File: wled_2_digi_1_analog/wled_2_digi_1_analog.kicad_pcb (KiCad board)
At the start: 2 copper layers, 100 x 38 mm, 54 parts, among them J1 Barrel_Jack_Switch, J2 Screw_Terminal_01x01, J3 Screw_Terminal_01x04, J4 Screw_Terminal_01x04, J5 Screw_Terminal_01x05, Q1 IRLR7843TR(UMW), Q2 AP15P04S, Q3 MMBT4401LT1G, Q4 MMBT4401LT1G, Q5 AP15P04S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

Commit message: Mounting Holes and 2pin connector
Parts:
- removed the ? at (111.0, 89.1)
- removed the ? at (102.0, 55.6)
- removed the ? at (139.5, 89.2)
- removed J2: Screw_Terminal_01x01, NicosLib:CONN-TH_P5.00_KF301-5.0-1P
- added ?: , , F.Cu at (70.2, 55.6)
- added ?: , , F.Cu at (102.1, 55.6)
- added ?: , , F.Cu at (139.5, 89.0)
- added U4: Screw Terminal, easyeda2kicad:CONN-TH_P5.00_KF301-5.0-2P, F.Cu at (71.5, 88.6)
- moved REF** 51.9 mm to (111.0, 89.0)
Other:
- board text added: "CH1"
- board text added: "CH2"
- board text added: "CH3"
- board text added: "CH4"
- board text added: "CH5"
- board text added: "V+ Analog"

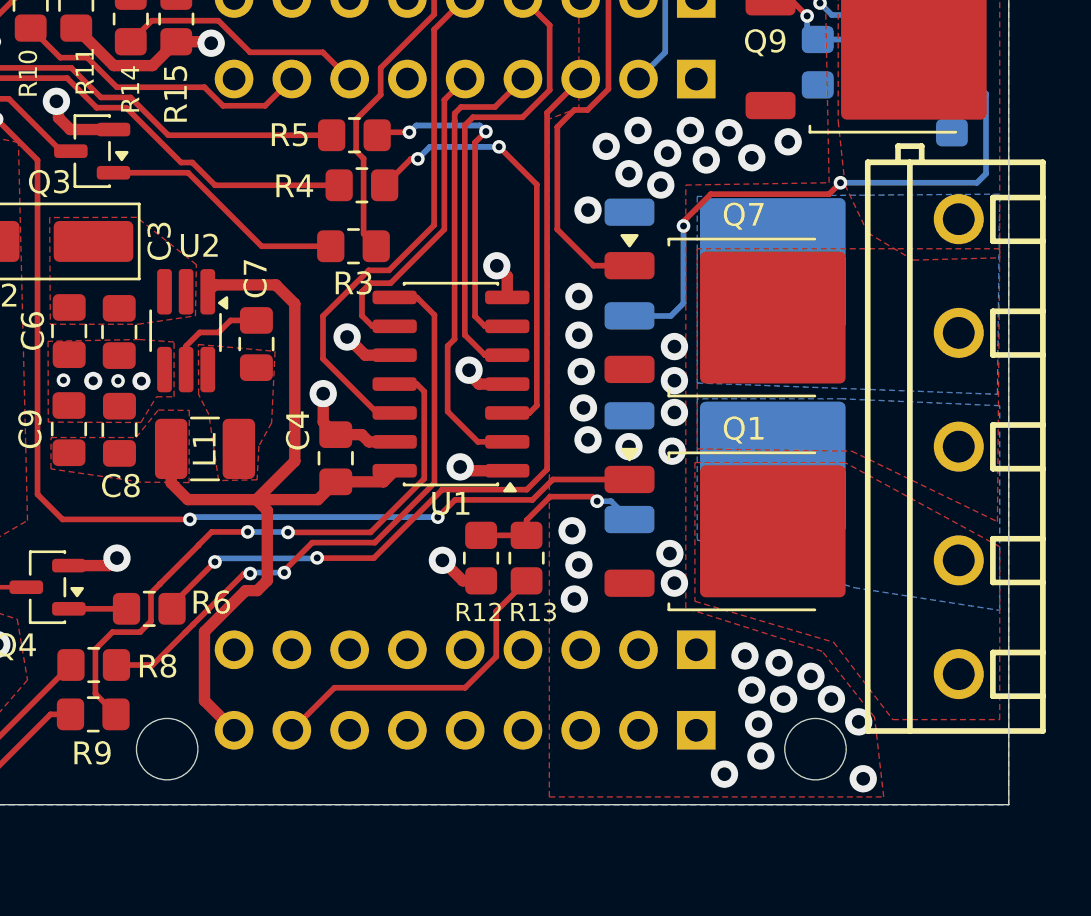
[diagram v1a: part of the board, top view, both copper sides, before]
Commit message: Switch 5pin to 2+3ping
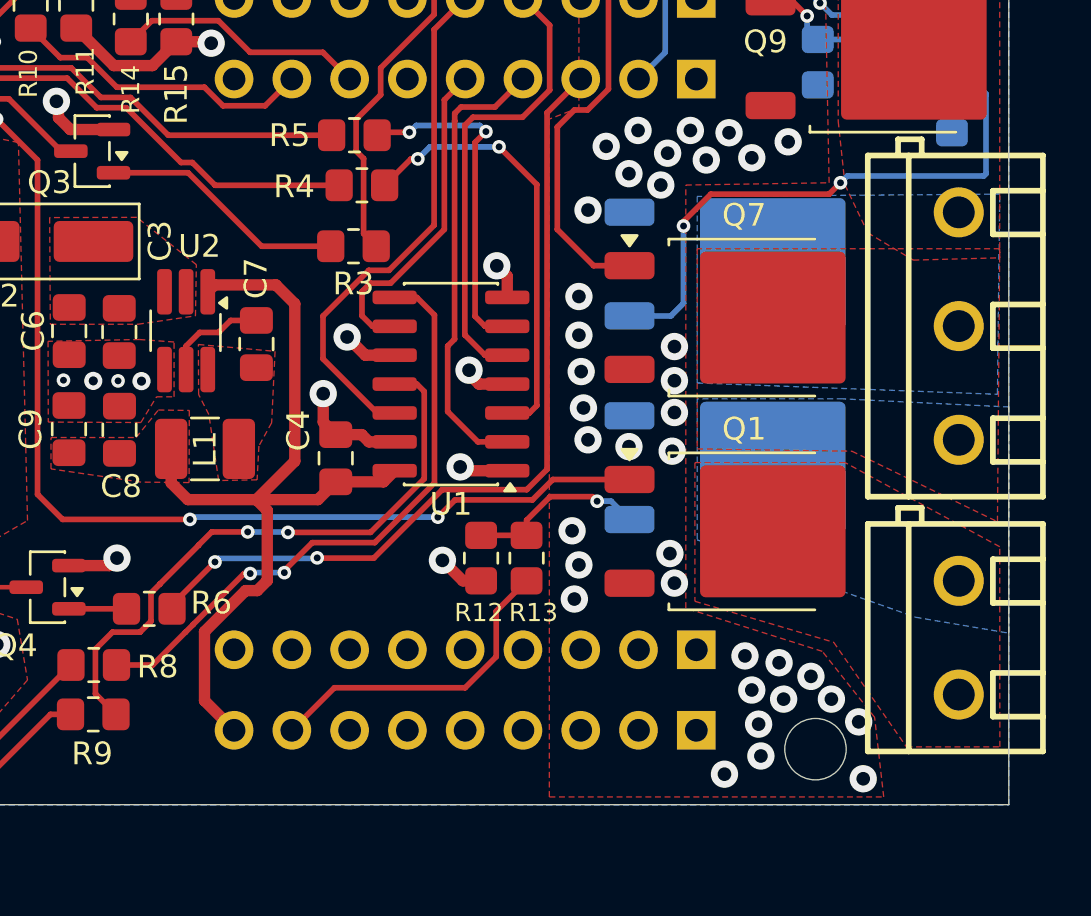
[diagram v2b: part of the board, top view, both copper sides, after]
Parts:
- removed J5: Screw_Terminal_01x05, NicosLib:CONN-TH_P5.00_KF301-5.0-5P
- removed REF**: MountingHole_2.7mm_M2.5_DIN965, MountingHole:MountingHole_2.7mm_M2.5_DIN965
- added J2: Screw_Terminal_01x03, NicosLib:CONN-TH_P5.00_KF301-5.0-3P, F.Cu at (145.8, 70.5)
- added U5: Screw Terminal, easyeda2kicad:CONN-TH_P5.00_KF301-5.0-2P, F.Cu at (145.8, 84.1)
